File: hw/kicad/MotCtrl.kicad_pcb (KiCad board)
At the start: 4 copper layers, 183.6 x 45.2 mm, 137 parts, among them P1 CONN_01X06, P2 CONN_01X03, P3 CONN_02X05, P4 CONN_01X05, Q1 FDBL0110N60, Q2 FDBL0110N60, Q3 FDBL0110N60, Q4 FDBL0110N60, Q5 FDBL0110N60, Q6 FDBL0110N60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

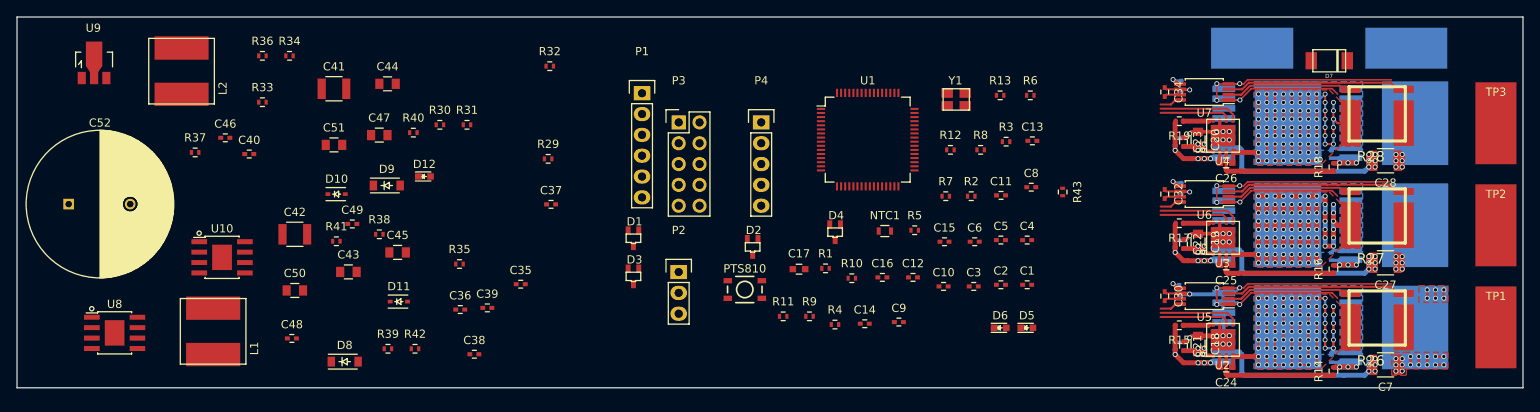
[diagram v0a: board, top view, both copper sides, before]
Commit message: Aligned, started rework current shunt layout and copper pour
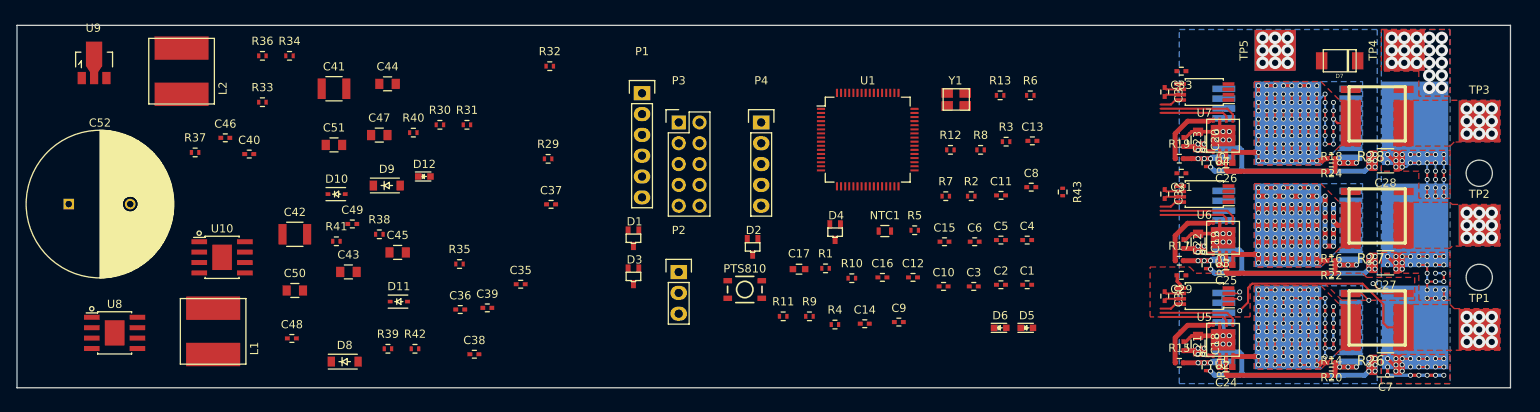
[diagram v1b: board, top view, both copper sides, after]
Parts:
- removed the TP1 at (200.7, 144.3)
- removed the TP2 at (200.7, 131.8)
- removed the TP3 at (200.7, 119.4)
- removed the TP4 at (189.7, 110.2)
- removed the TP5 at (170.9, 110.2)
- added REF**: MountingHole_3.2mm_M3, Mounting_Holes:MountingHole_3.2mm_M3, F.Cu at (198.6, 125.5)
- added REF**: MountingHole_3.2mm_M3, Mounting_Holes:MountingHole_3.2mm_M3, F.Cu at (198.6, 138.2)
- added TP1: Phase A, pads:SolderWirePad_single_SMD_5x5mm, B.Cu at (198.6, 144.5)
- added TP1: Phase A, pads:SolderWirePad_single_SMD_5x5mm, F.Cu at (198.6, 144.5)
- added TP2: Phase B, pads:SolderWirePad_single_SMD_5x5mm, B.Cu at (198.6, 131.8)
- added TP2: Phase B, pads:SolderWirePad_single_SMD_5x5mm, F.Cu at (198.6, 131.8)
- added TP3: Phase C, pads:SolderWirePad_single_SMD_5x5mm, B.Cu at (198.6, 119.1)
- added TP3: Phase C, pads:SolderWirePad_single_SMD_5x5mm, F.Cu at (198.6, 119.1)
- added TP4: Bat+, pads:SolderWirePad_single_SMD_5x5mm, F.Cu at (189.5, 110.5)
- added TP4: Bat+, pads:SolderWirePad_single_SMD_5x5mm, B.Cu at (189.5, 110.5)
- added TP5: Bat-, pads:SolderWirePad_single_SMD_5x5mm, F.Cu at (173.7, 110.5)
- added TP5: Bat-, pads:SolderWirePad_single_SMD_5x5mm, B.Cu at (173.7, 110.5)
- C29, C31, C33, R20, R21, R22, R23, R24, R25: moved to F.Cu
- moved R21 4.58 mm to (165.4, 149.1), turned to 270 degrees
- moved R25 4.58 mm to (165.4, 124.2), turned to 270 degrees
- moved R23 4.58 mm to (165.4, 136.7), turned to 270 degrees
- moved R15 4.57 mm to (162.1, 148.6), turned to 0 degrees
- moved R17 4.57 mm to (162.1, 136.1), turned to 0 degrees
- moved R19 4.57 mm to (162.1, 123.7), turned to 0 degrees
- moved C29 1.80 mm to (162.3, 137.9), turned to 180 degrees
- moved C31 1.78 mm to (162.3, 125.5), turned to 180 degrees
- moved C33 1.78 mm to (162.3, 113.0), turned to 180 degrees
- moved D7 1.27 mm to (181.6, 111.8)
- moved R14 0.57 mm to (180.6, 150.1), turned to 0 degrees
- moved R16 0.57 mm to (180.6, 137.7), turned to 0 degrees
- moved R18 0.57 mm to (180.6, 125.2), turned to 0 degrees
- moved R20 0.51 mm to (180.6, 148.6), turned to 180 degrees
- moved R22 0.51 mm to (180.6, 136.1), turned to 180 degrees
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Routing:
- net GND: track 297.1 -> 178.6 mm, vias 54 -> 48
- net VPP: track 82.4 -> 152.1 mm, vias 34 -> 103
- net /Power FET/MOT_PH_A: track 0.00 -> 50.5 mm, vias 0 -> 10
- net /Power FET/MOT_PH_C: track 0.00 -> 22.6 mm, vias 0 -> 9
- net Net-(R28-Pad4): track 22.2 -> 0.00 mm
- net Net-(R27-Pad4): track 22.0 -> 0.00 mm
- net /Power FET/MOT_PH_B: track 0.00 -> 20.4 mm, vias 0 -> 9
- net Net-(R27-Pad3): track 15.6 -> 0.00 mm
- net Net-(R28-Pad3): track 15.6 -> 0.00 mm
- net /Power FET/PH_A: track 122.7 -> 130.7 mm, vias 85 -> 94
- net Net-(R26-Pad3): track 15.5 -> 23.3 mm, vias 0 -> 2
- net /Power FET/PH_B: track 120.1 -> 127.2 mm, vias 85 -> 93
- net /Power FET/PH_C: track 118.7 -> 125.7 mm, vias 85 -> 93
- net Net-(Q2-Pad1): track 13.8 -> 8.22 mm, vias 4 -> 3
- net Net-(Q4-Pad1): track 14.1 -> 8.53 mm, vias 4 -> 3
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- added copper zone on F.Cu, net /Power FET/MOT_PH_A
- added copper zone on F.Cu, net /Power FET/MOT_PH_B
- added copper zone on F.Cu, net /Power FET/MOT_PH_C
- added copper zone on B.Cu, net GND
- added copper zone on F.Cu, net GND
- added copper zone on B.Cu, net VPP
- added copper zone on In2.Cu, net VPP
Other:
- board size 183.6 x 45.2 mm -> 182.1 x 44.2 mm

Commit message: First draft of power stage placed and routed
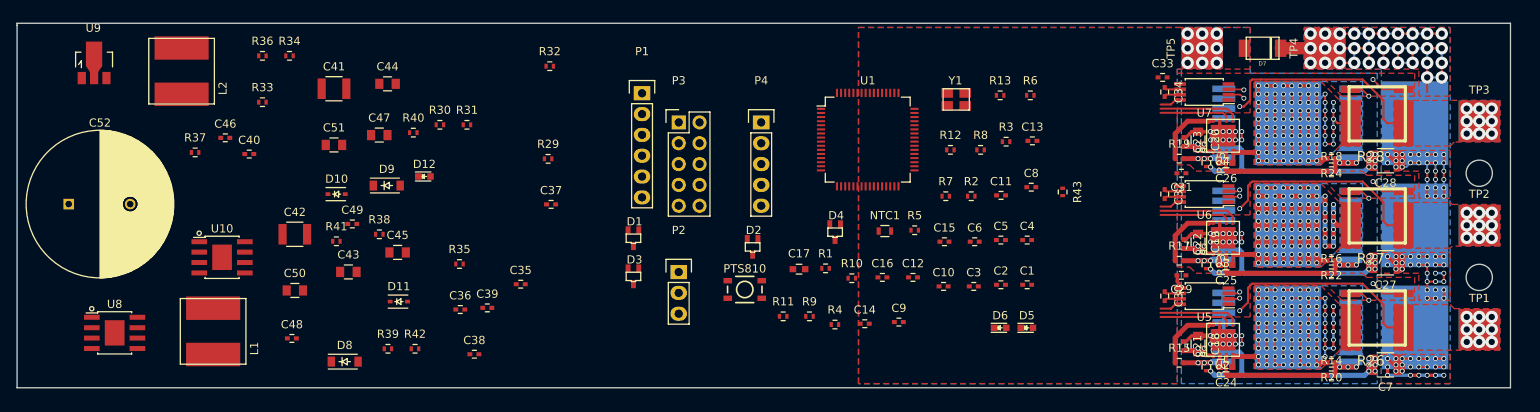
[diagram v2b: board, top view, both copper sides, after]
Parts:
- moved TP4 9.66 mm to (179.8, 110.2) (x2)
- moved D7 9.52 mm to (172.2, 110.2)
- moved TP5 8.89 mm to (164.8, 110.2) (x2)
- moved C33 2.41 mm to (160.0, 113.8), turned to 0 degrees
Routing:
- net VPP: track 152.1 -> 203.5 mm, vias 103 -> 116
- net /Power FET/MOT_PH_C: track 22.6 -> 59.0 mm, vias 9 -> 10
- net /Power FET/MOT_PH_B: track 20.4 -> 56.6 mm, vias 9 -> 10
- net Net-(R27-Pad4): track 0.00 -> 23.6 mm, vias 0 -> 2
- net Net-(R27-Pad3): track 0.00 -> 23.4 mm, vias 0 -> 2
- net Net-(R28-Pad3): track 0.00 -> 23.1 mm, vias 0 -> 2
- net Net-(R28-Pad4): track 0.00 -> 23.1 mm, vias 0 -> 2
- net GND: track 178.6 -> 197.0 mm, vias 48 -> 66
- added copper zone on In2.Cu, net GND
- added copper zone on In1.Cu, net VPP
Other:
- board size 182.1 x 44.2 mm -> 182.1 x 44.5 mm

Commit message: Changed footprint of and placed bulk cap
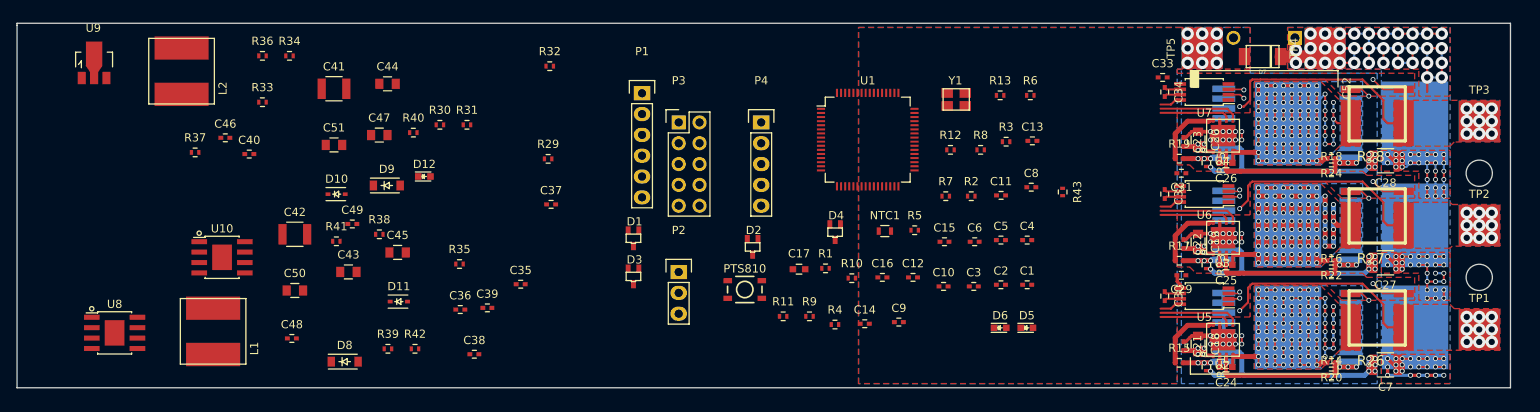
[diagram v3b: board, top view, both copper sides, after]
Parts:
- C52: footprint Capacitors_ThroughHole:C_Radial_D18_L36_P7.5 -> Capacitors_angled:C_Radial_D18_L37_P7.5_Angled
- moved C52 143.5 mm to (168.7, 109.0)
- moved D7 1.02 mm to (172.2, 111.3)
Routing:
- net VPP: track 203.5 -> 209.9 mm, vias 116 -> 118

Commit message: Placing power supply components
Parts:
- C48, C49, R38, R40, R41: moved to B.Cu
- moved R37 114.7 mm to (156.7, 121.9)
- moved R36 108.5 mm to (156.5, 133.3)
- moved C40 108.1 mm to (156.7, 123.4)
- moved U10 107.5 mm to (151.4, 118.1), turned to 90 degrees
- moved R33 106.5 mm to (156.7, 120.4)
- moved U8 106.1 mm to (134.9, 118.1), turned to 90 degrees
- moved L2 103.4 mm to (143.8, 113.3)
- moved R34 103.3 mm to (156.7, 115.8), turned to 180 degrees
- moved U9 99.1 mm to (127.8, 126.5), turned to 180 degrees
- moved C43 94.6 mm to (152.1, 113.0), turned to 180 degrees
- moved C41 93.8 mm to (152.7, 110.2), turned to 180 degrees
- moved R41 92.9 mm to (151.4, 121.4)
- moved L1 88.8 mm to (127.3, 113.3)
- moved C49 88.7 mm to (148.8, 118.1), turned to 270 degrees
- moved C51 87.1 mm to (146.1, 118.9), turned to 180 degrees
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
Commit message: Changed footprint of hall sensor contact and placed more components
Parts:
- added REF**: MountingHole_3.2mm_M3, Mounting_Holes:MountingHole_3.2mm_M3, F.Cu at (129.5, 148.1)
- added REF**: MountingHole_3.2mm_M3, Mounting_Holes:MountingHole_3.2mm_M3, F.Cu at (198.9, 110.7)
- added REF**: MountingHole_3.2mm_M3, Mounting_Holes:MountingHole_3.2mm_M3, F.Cu at (129.5, 111.0)
- C35, C36, C37, C38, C39, C40, D2, D3, D4, NTC1, R29, R30, R31, R32, R33, R34, R35, R36, R37: moved to B.Cu
- P1: footprint Pin_Headers:Pin_Header_Straight_1x06 -> Micro_JST:Micro_JST_p2.0_6
- moved NTC1 83.2 mm to (167.4, 125.6)
- moved SW1 63.5 mm to (129.8, 127.8), turned to 180 degrees
- moved R12 44.9 mm to (136.7, 130.8)
- moved R13 42.0 mm to (136.7, 133.6)
- moved D6 36.9 mm to (133.9, 133.6)
- moved D1 35.9 mm to (86.6, 118.9)
- moved D5 33.5 mm to (133.9, 130.8)
- moved R34 33.5 mm to (157.2, 149.4)
- moved C37 30.5 mm to (157.2, 147.8)
- moved C38 26.9 mm to (157.2, 119.6)
- moved P4 26.6 mm to (159.3, 149.4)
- moved R33 24.4 mm to (157.2, 144.8)
- moved R35 23.9 mm to (157.2, 121.2)
- moved R37 21.3 mm to (157.2, 143.3)
- moved R29 20.9 mm to (157.2, 122.7)
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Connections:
- P1 pad 1: +5V -> GND
- P1 pad 2: /Microcontroller/MOT_TEMP -> Net-(P1-Pad2)
- P1 pad 5: Net-(P1-Pad5) -> /Microcontroller/MOT_TEMP
- P1 pad 6: GND -> +5V
- R10 pad 2: Net-(P1-Pad4) -> Net-(P1-Pad3)
- R11 pad 2: Net-(P1-Pad3) -> Net-(P1-Pad4)
- R4 pad 2: Net-(P1-Pad5) -> Net-(P1-Pad2)
- R6 pad 2: Net-(P1-Pad4) -> Net-(P1-Pad3)
- R7 pad 2: Net-(P1-Pad3) -> Net-(P1-Pad4)
- R9 pad 2: Net-(P1-Pad5) -> Net-(P1-Pad2)
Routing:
- net /Microcontroller/BOARD_TEMP: track 0.00 -> 12.0 mm, vias 0 -> 1
- net +3V3: track 1.92 -> 9.07 mm, vias 0 -> 2
- net GND: track 197.0 -> 192.9 mm

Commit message: Routed power supply
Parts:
- P1: footprint Micro_JST:Micro_JST_p2.0_6 -> JST_ZH:JST_ZH_B6B-ZR
- R12, R13: moved to B.Cu
- moved C12 63.8 mm to (151.6, 134.9)
- moved C13 52.7 mm to (151.6, 140.5)
- moved Y1 35.8 mm to (152.1, 137.7), turned to 270 degrees
- moved C38 13.2 mm to (147.1, 128.0)
- moved R35 10.1 mm to (149.9, 128.0)
- moved R29 7.97 mm to (149.9, 125.7)
- moved D6 6.27 mm to (128.5, 130.3)
- moved R41 6.10 mm to (147.8, 121.2), turned to 270 degrees
- moved R13 6.06 mm to (131.6, 130.3)
- moved D5 5.48 mm to (128.5, 132.1)
- moved R12 5.24 mm to (131.6, 132.1)
- moved R40 4.68 mm to (149.4, 121.2), turned to 270 degrees
- moved U1 4.33 mm to (143.8, 136.1)
- moved P1 1.80 mm to (128.5, 138.4), turned to 270 degrees
- moved R38 1.44 mm to (141.2, 114.3)
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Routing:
- net GND: track 192.9 -> 299.1 mm, vias 66 -> 123
- net +5V: track 0.00 -> 73.5 mm, vias 0 -> 25
- net +3V3: track 9.07 -> 62.1 mm, vias 2 -> 12
- net VPP: track 209.9 -> 255.5 mm, vias 118 -> 131
- net +12V: track 38.7 -> 65.5 mm, vias 12 -> 34
- net Net-(C49-Pad1): track 0.00 -> 12.2 mm, vias 0 -> 1
- net Net-(C48-Pad1): track 0.00 -> 10.6 mm, vias 0 -> 1
- net Net-(R40-Pad2): track 0.00 -> 9.15 mm, vias 0 -> 1
- net /Microcontroller/BTN: track 0.00 -> 4.20 mm
- net Net-(C48-Pad2): track 0.00 -> 2.88 mm, vias 0 -> 1
- net Net-(C49-Pad2): track 0.00 -> 2.53 mm, vias 0 -> 1
- net /Microcontroller/BOARD_TEMP: track 12.0 -> 10.1 mm, vias 1 -> 2
- net Net-(R38-Pad1): track 0.00 -> 1.97 mm, vias 0 -> 1
- net Net-(D12-Pad2): track 0.00 -> 1.59 mm
- net /Microcontroller/PWM_H_C: track 9.82 -> 10.9 mm
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- added copper zone on B.Cu, net +12V
- added copper zone on F.Cu, net +12V
- added copper zone on In1.Cu, net +12V
- added copper zone on B.Cu, net +5V
- added copper zone on F.Cu, net +5V
- added copper zone on F.Cu, net Net-(C48-Pad1)
- added copper zone on F.Cu, net Net-(C49-Pad1)

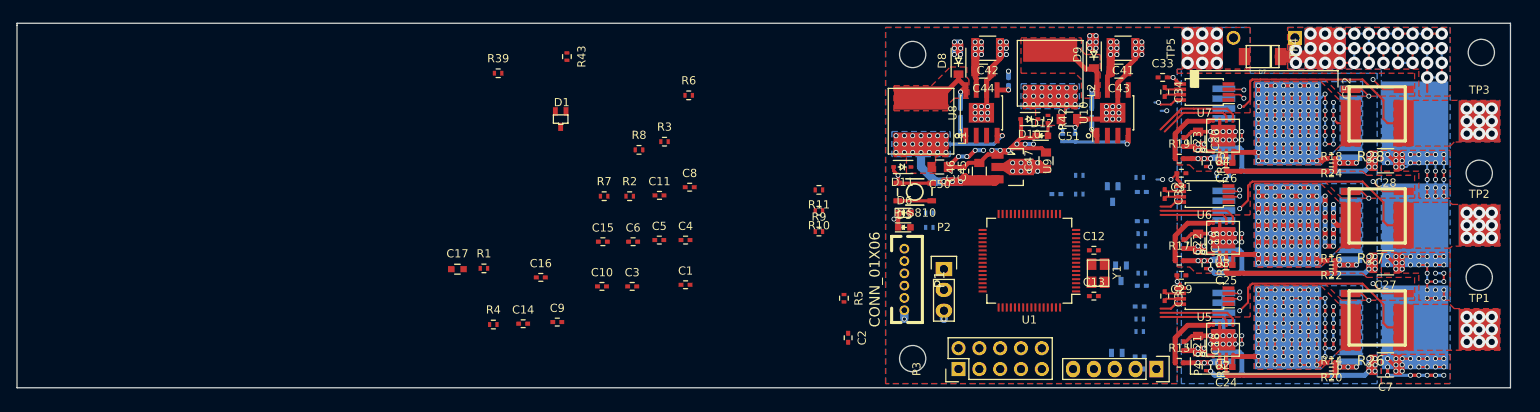
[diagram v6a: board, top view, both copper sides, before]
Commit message: Routed EMF and I sense to mcu
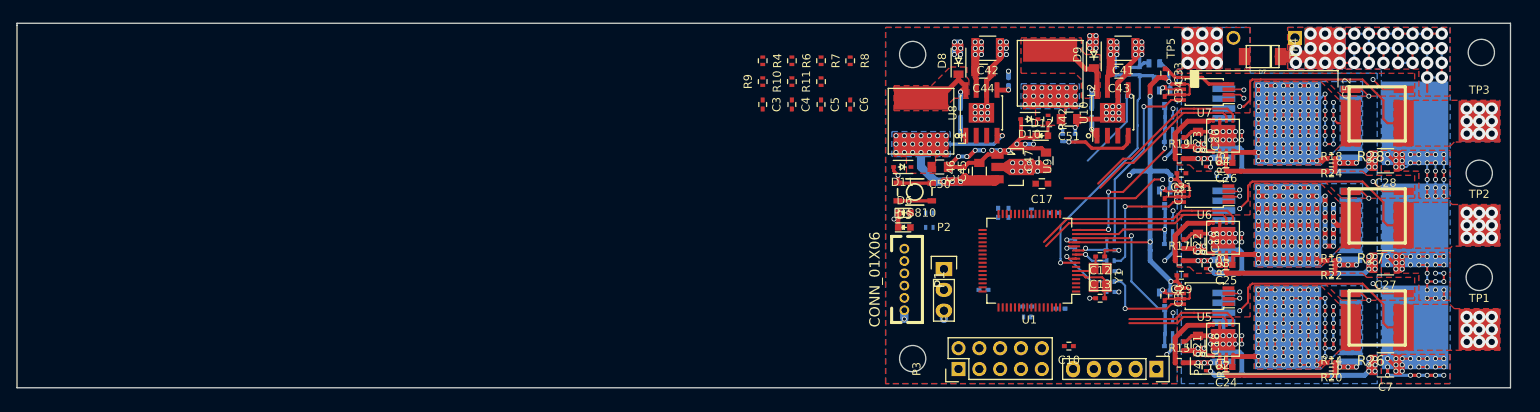
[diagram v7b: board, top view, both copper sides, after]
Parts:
- removed R43: 0R, Resistors_SMD:R_0402
- C1, C11, C14, C15, C16, C2, C8, C9, D1, R1, R2, R3, R39, R5: moved to B.Cu
- moved R1 80.6 mm to (154.2, 113.0), turned to 90 degrees
- moved R39 76.3 mm to (155.2, 116.1)
- moved D1 72.6 mm to (159.0, 113.0), turned to 180 degrees
- moved C17 72.0 mm to (145.3, 126.7), turned to 180 degrees
- moved C9 63.9 mm to (149.4, 134.1), turned to 270 degrees
- moved C16 63.1 mm to (146.8, 130.3)
- moved R2 62.6 mm to (155.7, 113.0), turned to 90 degrees
- moved C1 61.2 mm to (157.2, 113.0), turned to 90 degrees
- moved C10 57.4 mm to (148.6, 146.6), turned to 180 degrees
- moved C14 56.3 mm to (138.2, 139.7), turned to 180 degrees
- moved C11 50.8 mm to (147.6, 142.0), turned to 180 degrees
- moved C15 48.3 mm to (140.0, 130.3), turned to 270 degrees
- moved R4 46.0 mm to (111.3, 111.8), turned to 270 degrees
- moved R3 45.6 mm to (144.0, 130.3), turned to 270 degrees
- moved C8 39.0 mm to (141.2, 130.3), turned to 270 degrees
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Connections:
- C30 pad 2: /Power FET/I_SENSE_V_REF -> +3V3
- C32 pad 2: /Power FET/I_SENSE_V_REF -> +3V3
- C34 pad 2: /Power FET/I_SENSE_V_REF -> +3V3
- C9 pad 1: /Power FET/I_SENSE_V_REF -> +3V3
- U1 pad 13: /Power FET/I_SENSE_V_REF -> +3V3
- U5 pad 7: /Power FET/I_SENSE_V_REF -> +3V3
- U6 pad 7: /Power FET/I_SENSE_V_REF -> +3V3
- U7 pad 7: /Power FET/I_SENSE_V_REF -> +3V3
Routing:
- net +3V3: track 62.1 -> 132.5 mm, vias 12 -> 16
- net GND: track 299.1 -> 335.0 mm, vias 123 -> 134
- net /Microcontroller/BAT_SENSE: track 0.00 -> 34.1 mm, vias 0 -> 1
- net /Microcontroller/V_EMF_SENSE_C: track 0.00 -> 23.2 mm, vias 0 -> 3
- net /Microcontroller/V_EMF_SENSE_A: track 0.00 -> 22.6 mm, vias 0 -> 1
- net Net-(R34-Pad1): track 3.48 -> 23.2 mm
- net /Microcontroller/V_EMF_SENSE_B: track 0.00 -> 16.2 mm, vias 0 -> 1
- net /Microcontroller/PWM_H_B: track 9.82 -> 25.6 mm
- net /Microcontroller/PWM_L_B: track 8.68 -> 24.2 mm
- net Net-(R32-Pad1): track 2.61 -> 15.3 mm, vias 0 -> 1
- net /Microcontroller/BOARD_TEMP: track 10.1 -> 22.2 mm
- net /Microcontroller/GATE_PWR_EN: track 0.00 -> 12.0 mm, vias 0 -> 1
- net /Microcontroller/PWM_L_C: track 9.12 -> 19.8 mm
- net /Microcontroller/PWM_H_C: track 10.9 -> 21.2 mm
- net /Microcontroller/I_SENS_A: track 0.00 -> 8.94 mm, vias 0 -> 1
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
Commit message: First draft of completely routed board
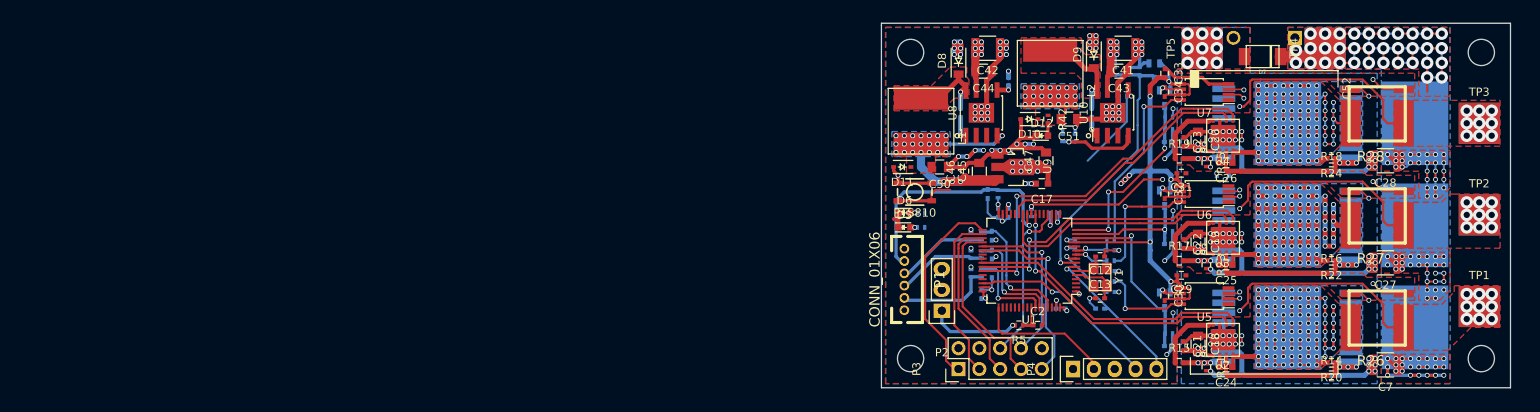
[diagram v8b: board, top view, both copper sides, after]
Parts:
- removed the REF** at (198.6, 125.5)
- C10, C3, C4, C5, C6, R10, R11, R4, R6, R7, R8, R9: moved to B.Cu
- C2, R5: moved to F.Cu
- moved R4 36.3 mm to (136.7, 137.7)
- moved R9 35.5 mm to (137.9, 137.7), turned to 270 degrees
- moved C3 34.7 mm to (139.2, 137.7)
- moved R6 32.2 mm to (136.7, 135.4)
- moved R10 31.3 mm to (137.9, 135.4), turned to 270 degrees
- moved C4 30.5 mm to (139.2, 135.4)
- moved R7 28.1 mm to (136.7, 133.1)
- moved R11 27.1 mm to (137.9, 133.1), turned to 270 degrees
- moved C5 26.3 mm to (139.2, 133.1)
- moved R8 24.3 mm to (140.0, 128.0), turned to 90 degrees
- moved C6 20.0 mm to (138.7, 128.0)
- moved P4 10.2 mm to (149.1, 149.4), turned to 90 degrees
- moved REF** 9.91 mm to (198.9, 148.1)
- moved C10 5.95 mm to (152.4, 142.0)
- moved P2 5.09 mm to (133.1, 142.2), turned to 180 degrees
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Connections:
- P3 pad 2: +3V3 -> +5V
- P3 pad 4: +5V -> +3V3
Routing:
- net /Microcontroller/MOT_TEMP: track 0.00 -> 30.8 mm, vias 0 -> 1
- net /Microcontroller/EXT_NSS_CANRX: track 0.00 -> 25.2 mm
- net /Microcontroller/SWDIO: track 0.00 -> 24.4 mm, vias 0 -> 1
- net /Microcontroller/PWM_H_C: track 21.2 -> 45.4 mm, vias 0 -> 2
- net /Microcontroller/EXT_SDA_SCK_RX: track 0.00 -> 23.0 mm, vias 0 -> 1
- net /Microcontroller/EXT_MOSI: track 0.00 -> 21.6 mm
- net /Microcontroller/PWM_L_A: track 12.8 -> 34.1 mm, vias 0 -> 2
- net /Microcontroller/PWM_H_A: track 13.9 -> 35.0 mm
- net /Microcontroller/EXT_SCK_CANTX: track 0.00 -> 20.6 mm
- net /Microcontroller/EXT_MISO: track 0.00 -> 20.6 mm
- net /Microcontroller/EXT_SCL_TX: track 0.00 -> 20.3 mm, vias 0 -> 1
- net /Microcontroller/EXT_ADC_DAC: track 0.00 -> 19.7 mm, vias 0 -> 1
- net /Microcontroller/RST: track 0.00 -> 18.8 mm, vias 0 -> 1
- net +3V3: track 132.5 -> 151.3 mm, vias 16 -> 26
- net GND: track 335.0 -> 353.6 mm, vias 134 -> 139
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- added copper zone on In1.Cu, net +3V3
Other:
- board size 182.1 x 44.5 mm -> 76.7 x 44.5 mm
